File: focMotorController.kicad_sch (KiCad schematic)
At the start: 0 parts

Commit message: Start creating schematic
Currently includes:
- Power input circuitry and filtering
- Logic: microcontroller and encoder connection
- Level shifters for encoder
- Status LEDs
- Output MOSFETs
- MOSFET gate drivers with appropriate filtering (I think...)

A few other things are a work-in-porogress, like current sensing.
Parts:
- added A1: Arduino Nano RP2040 Connect, Module:Arduino_Nano, symbol MCU_Module:Arduino_Nano_RP2040_Connect
- added C1: 470uF electrolytic, symbol Device:C
- added C2: 0.1uF ceramic, symbol Device:C
- added C3: Bootstrap A 0.1uF/25v, symbol Device:C
- added C4: Bootstrap B 0.1uF/25v, symbol Device:C
- added C5: Bootstrap C 0.1uF/25v, symbol Device:C
- added C6: Deboupling B 1uF/25V, symbol Device:C
- added C7: Deboupling A 1uF/25V, symbol Device:C
- added C8: Deboupling C 1uF/25V, symbol Device:C
- added D1: SMAJ15A - TVS diode for voltage spike protection, Diode_SMD:D_SMA, symbol Diode:SMAJ15A
- added D2, D7, D8, D9: STPS20L15D, Footprints:STPS20L15D, symbol Device:D
- added D3: Power LED (red), symbol Device:LED
- added D4: Status LED 1 (green), symbol Device:LED
- added D5: Status LED 2 (green), symbol Device:LED
- added D6: Status LED 3 (green), symbol Device:LED
- added F1: Resettable polyfuse for overcurrent protection, symbol Device:Polyfuse
- added J2: JST-PH encoder connection, symbol Connector:Conn_01x06_Pin
- added P1: WJ128V-5.0-3P, Footprints:WJ128V-5.0-3P, symbol WJ128V-5.0-3P:WJ128V-5.0-3P
- added P2: Power input, Footprints:WJ128V-5.0-2P, symbol WJ128V-5.0-2P:WJ128V-5.0-2P
- added R1: 3.3k, symbol Device:R_Small
- added R10: Gate BL 20ohm, symbol Device:R
- added R11, R13, R7, R8: Pulldown 47k, symbol Device:R_Small
- added R12: Gate CH 20ohm, symbol Device:R
- added R19: Gate AL 20ohm, symbol Device:R
- added R2: 2k, symbol Device:R_Small
- added R20: Gate CL 20ohm, symbol Device:R
- added R22: Gate AH 20ohm, symbol Device:R
- added R3: 620ohm, symbol Device:R_Small
- added R4, R5, R6: 100ohm, symbol Device:R_Small
- added R9: Gate BH 20ohm, symbol Device:R
- added U1, U2: 74LVC2T45DC, Package_SO:VSSOP-8_2.3x2mm_P0.5mm, symbol Logic_LevelTranslator:74LVC2T45DC
- added U10: IR2104 Gate Driver B, symbol Driver_FET:IR2104
- added U11: IR2104 Gate Driver C, symbol Driver_FET:IR2104
- added U3: MOSFET A low, Footprints:STP55NF06L, symbol STP55NF06L:STP55NF06L
- added U4: MOSFET B low, Footprints:STP55NF06L, symbol STP55NF06L:STP55NF06L
- added U5: MOSFET C low, Footprints:STP55NF06L, symbol STP55NF06L:STP55NF06L
- added U6: MOSFET A high, Footprints:STP55NF06L, symbol STP55NF06L:STP55NF06L
- added U7: MOSFET B high, Footprints:STP55NF06L, symbol STP55NF06L:STP55NF06L
- added U8: MOSFET C high, Footprints:STP55NF06L, symbol STP55NF06L:STP55NF06L
- added U9: IR2104 Gate Driver A, symbol Driver_FET:IR2104
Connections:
- new net: D2.2 (A), F1.2
- new net: R20.1, U11.5 (LO)
- new net: D3.2 (A), R3.2
- new net: R19.1, U9.5 (LO)
- new net: D6.2 (A), R6.2
- new net: J2.5 (Motor_Temperature), R1.1
- new net: A1.19 (A0), R1.2, R2.2
- new net: D4.2 (A), R4.2
- new net: C1.1, C2.2
- new net: D5.2 (A), R5.2
- new net: R10.1, U10.5 (LO)
- new net: R12.1, U11.7 (HO)
- new net: C5.1, D9.1 (K), U11.8 (VB)
- new net: R9.1, U10.7 (HO)
- new net: C4.1, D8.1 (K), U10.8 (VB)
- new net: C3.1, D7.1 (K), U9.8 (VB)
- new net: R22.1, U9.7 (HO)
- new net +12V: F1.1, P2.1
- new net 3.3VDD: A1.17 (3V3), U1.1 (VCCA), U2.1 (VCCA)
- new net 5VDD: A1.27 (VUSB/5V), J2.6 (+5V), R3.1, U1.8 (VCCB), U2.8 (VCCB)
- new net AHighGate: R22.2, U6.1
- new net ALowGate: R19.2, U3.1
- new net BHighGate: R9.2, U7.1
- new net BLowGate: R10.2, U4.1
- new net CHighGate: R12.2, U8.1
- new net CLowGate: R20.2, U5.1
- new net Enable: A1.14 (D11/COPI), C6.1, C8.1, R13.2, U10.3 (~{SD}), U11.3 (~{SD}), U9.3 (~{SD})
- new net EncLogicA: A1.5 (D2), U1.3 (2A)
- new net EncLogicB: A1.6 (D3), U2.2 (1A)
- new net EncLogicC: A1.7 (D4), U2.3 (2A)
- new net EncoderA: J2.4 (Encoder_A), U1.6 (2B)
- new net EncoderB: J2.3 (Encoder_B), U2.7 (1B)
- new net EncoderC: J2.2 (Encoder_C_/_Index), U2.6 (2B)
- new net GND: A1.29 (GND), A1.4 (GND), C2.1, C6.2, C7.2, C8.2, D1.1 (A1), D3.1 (K), D4.1 (K), D5.1 (K), D6.1 (K), J2.1 (Ground), P2.2, R11.1, R13.1, R2.1, R7.1, R8.1, U1.4 (GND), U1.5 (DIR), U10.4 (COM), U11.4 (COM), U2.4 (GND), U2.5 (DIR), U3.3, U4.3, U5.3, U9.4 (COM)
- new net PVIN: A1.30 (VIN), C1.2, C7.1, D1.2 (A2), D2.1 (K), D7.2 (A), D8.2 (A), D9.2 (A), U10.1 (VCC), U11.1 (VCC), U6.2, U7.2, U8.2, U9.1 (VCC)
- new net PhaseA: A1.11 (D8), R7.2, U9.2 (IN)
- new net PhaseAOut: C3.2, P1.1, U3.2, U6.3, U9.6 (VS)
- new net PhaseB: A1.12 (D9), R8.2, U10.2 (IN)
- new net PhaseBOut: C4.2, P1.2, U10.6 (VS), U4.2, U7.3
- new net PhaseC: A1.13 (D10/CS), R11.2, U11.2 (IN)
- new net PhaseCOut: C5.2, P1.3, U11.6 (VS), U5.2, U8.3
- new net Status1: A1.8 (D5), R4.1
- new net Status2: A1.9 (D6), R5.1
- new net Status3: A1.10 (D7), R6.1
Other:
- note added: "Can handle 5-18V input"
- note added: "DIR = LOW passes data B -> A"
- note added: "For my own reference lol V_out = V_in * R_2 / (R_1 + R_2) For 5V to 3.3V level shifting, R_2 / (R_1 + R_2) = 3.3 / 5, so e.g R_1 = 3.3k / R_2 = 2k"
- note added: "Level shifters (forced 5V to 3.3V)"
- note added: "Logic"
- note added: "MOSFET Gate Drivers"
- note added: "Note: Gate resistors should be placed directly before the MOSFET gate pin to reduce PCB loop inductance"
- note added: "Output MOSFETs"
- note added: "Power input"
- note added: "Regulated outputs"
- note added: "Should handle ~10A hold current"
- note added: "Status LEDs"
- note added: "VCC deboupling and bootstrap capacitors should also be directly next to the gate driver ICs"

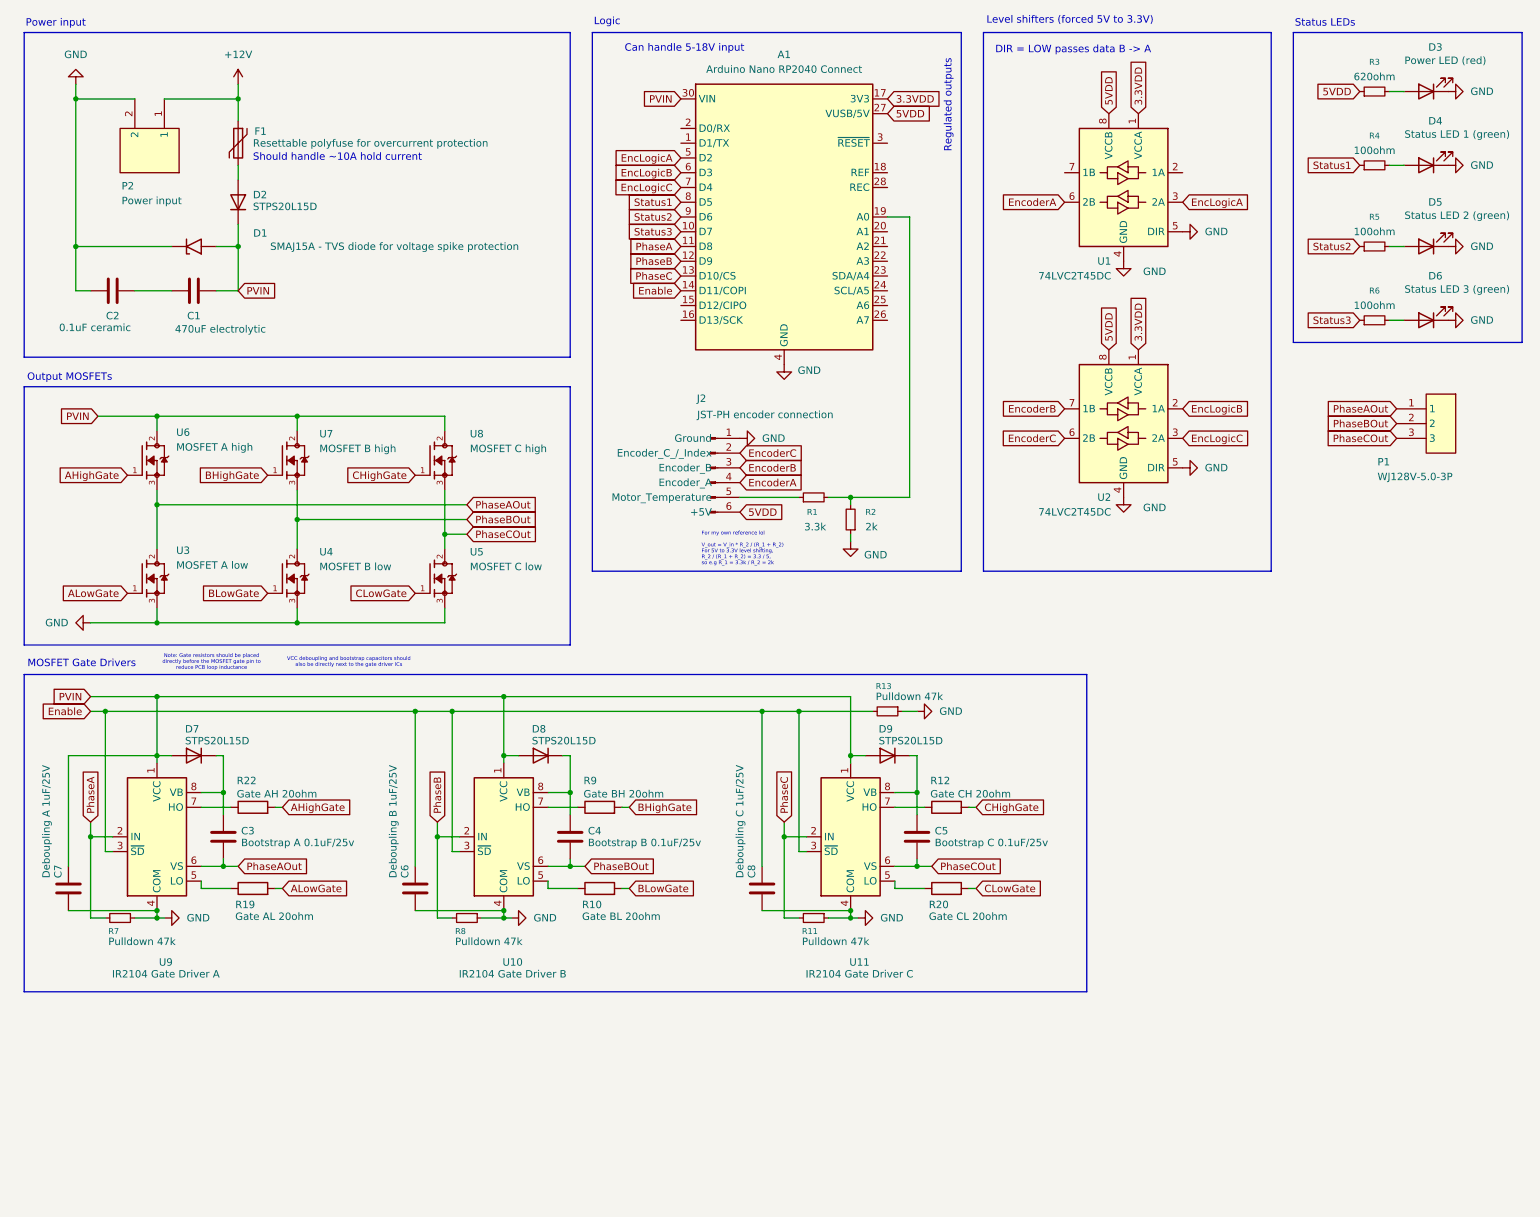
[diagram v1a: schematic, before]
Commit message: Add current sensing circuitry
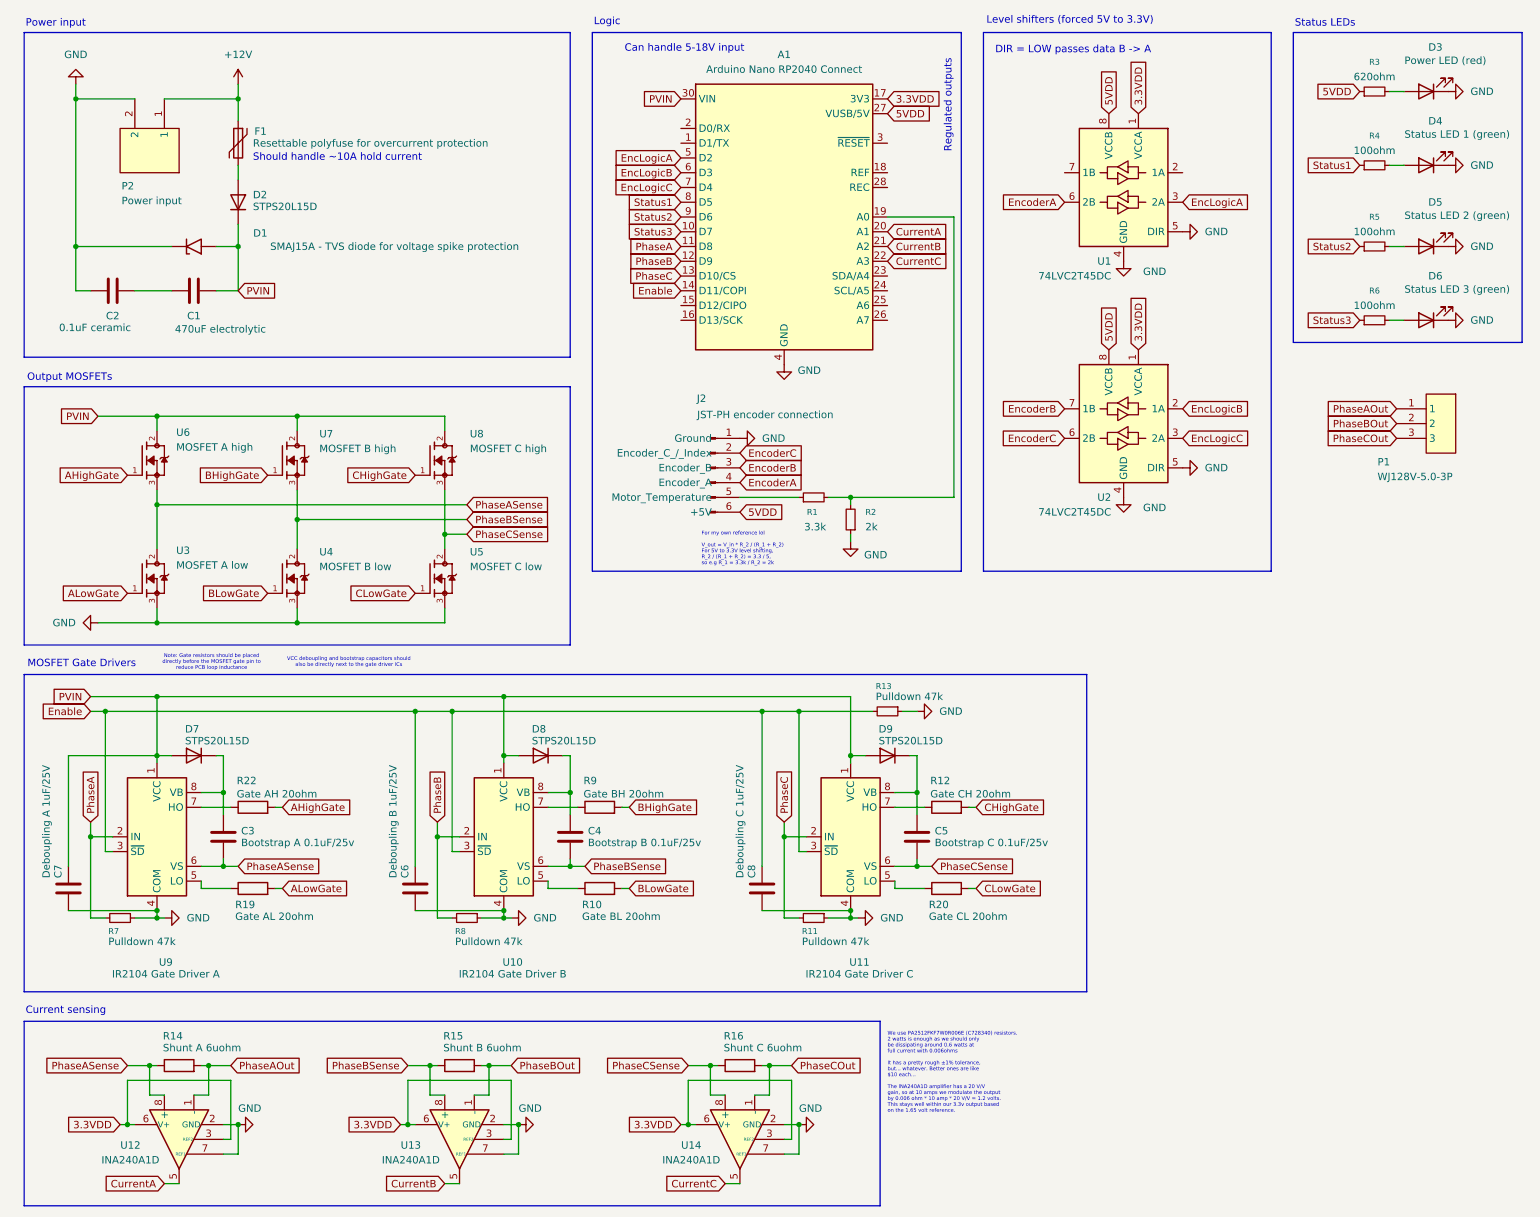
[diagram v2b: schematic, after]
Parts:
- added R14: Shunt A 6uohm, Resistor_SMD:R_2512_6332Metric, symbol Device:R
- added R15: Shunt B 6uohm, Resistor_SMD:R_2512_6332Metric, symbol Device:R
- added R16: Shunt C 6uohm, Resistor_SMD:R_2512_6332Metric, symbol Device:R
- added U12, U13, U14: INA240A1D, Package_SO:SOIC-8_3.9x4.9mm_P1.27mm, symbol Amplifier_Current:INA240A1D
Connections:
- net 3.3VDD: now also U12.3 (REF2), U12.6 (V+), U13.3 (REF2), U13.6 (V+), U14.3 (REF2), U14.6 (V+)
- net GND: now also U12.2 (GND), U12.4 (GND), U12.7 (REF1), U13.2 (GND), U13.4 (GND), U13.7 (REF1), U14.2 (GND), U14.4 (GND), U14.7 (REF1)
- net PhaseAOut: now also R14.2, U12.1 (-); no longer C3.2, U3.2, U6.3, U9.6 (VS)
- net PhaseBOut: now also R15.2, U13.1 (-); no longer C4.2, U10.6 (VS), U4.2, U7.3
- net PhaseCOut: now also R16.2, U14.1 (-); no longer C5.2, U11.6 (VS), U5.2, U8.3
- net CurrentA: now reaches A1.20 (A1)
- net CurrentA: now also U12.5
- net CurrentB: now reaches A1.21 (A2)
- net CurrentB: now also U13.5
- net CurrentC: now reaches A1.22 (A3)
- net CurrentC: now also U14.5
- new net PhaseASense: C3.2, R14.1, U12.8 (+), U3.2, U6.3, U9.6 (VS)
- new net PhaseBSense: C4.2, R15.1, U10.6 (VS), U13.8 (+), U4.2, U7.3
- new net PhaseCSense: C5.2, R16.1, U11.6 (VS), U14.8 (+), U5.2, U8.3
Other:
- note added: "Current sensing"
- note added: "We use PA2512FKF7W0R006E (C728340) resistors. 2 watts is enough as we should only be dissipating around 0.6 watts at full current with 0.006ohms It has a pretty rough ±1% tolerance, but... whatever. Better ones are like $10 each... The INA240A1D amplifier has a 20 V/V gain, so at 10 amps we modulate the output by 0.006 ohm * 10 amp * 20 V/V = 1.2 volts. This stays well within our 3.3v output base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"

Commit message: Finish initial routing
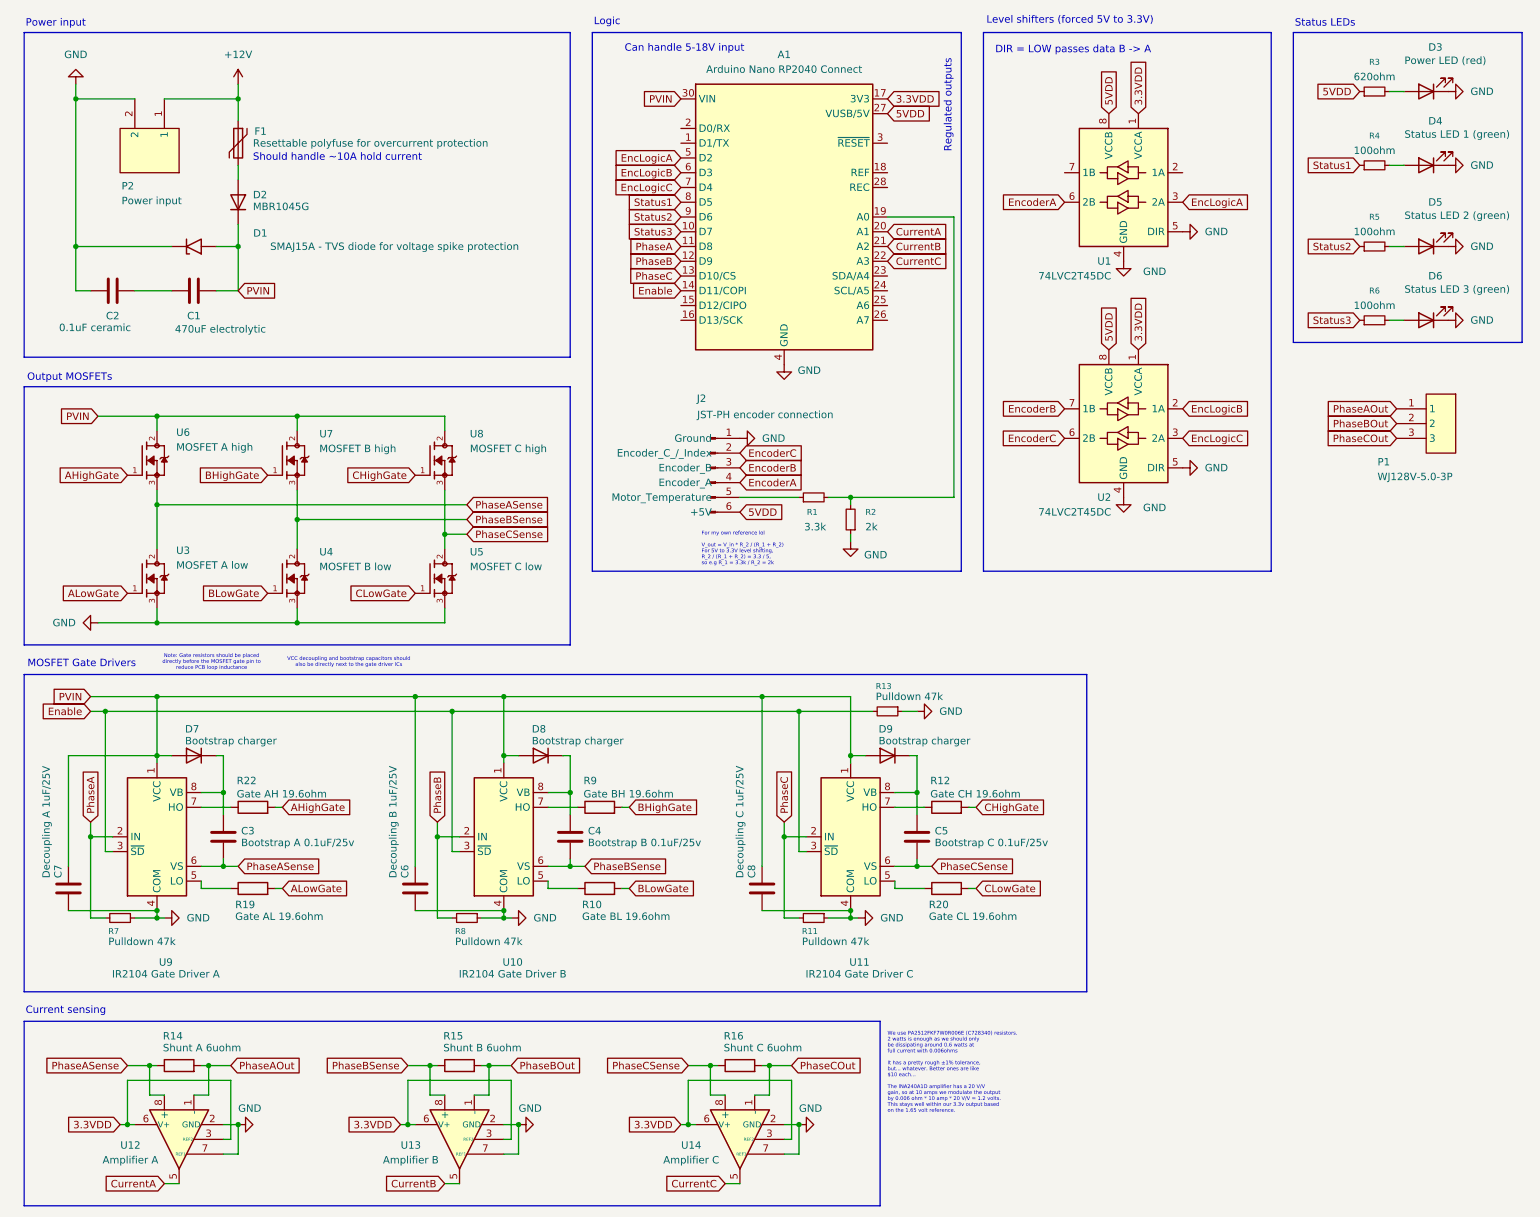
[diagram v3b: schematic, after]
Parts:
- C1: footprint (none) -> Capacitor_THT:CP_Radial_D8.0mm_P3.50mm
- C2, C3, C4, C5: footprint (none) -> Capacitor_THT:C_Disc_D5.0mm_W2.5mm_P5.00mm
- C6: value Deboupling B 1uF/25V -> Decoupling B 1uF/25V; footprint (none) -> Capacitor_THT:CP_Radial_D5.0mm_P2.00mm
- C7: value Deboupling A 1uF/25V -> Decoupling A 1uF/25V; footprint (none) -> Capacitor_THT:CP_Radial_D5.0mm_P2.00mm
- C8: value Deboupling C 1uF/25V -> Decoupling C 1uF/25V; footprint (none) -> Capacitor_THT:CP_Radial_D5.0mm_P2.00mm
- D2: value STPS20L15D -> MBR1045G; footprint Footprints:STPS20L15D -> Package_TO_SOT_THT:TO-220-2_Vertical
- D3, D4, D5, D6, R1, R11, R13, R2, R3, R4, R5, R6, R7, R8: footprint (none) -> LED_SMD:LED_1206_3216Metric
- D7, D8, D9: value STPS20L15D -> Bootstrap charger; footprint Footprints:STPS20L15D -> Diode_SMD:D_SOD-123
- F1: footprint (none) -> Footprints:A16-1000
- J2: footprint (none) -> Connector_JST:JST_PH_S6B-PH-K_1x06_P2.00mm_Horizontal
- R10: value Gate BL 20ohm -> Gate BL 19.6ohm; footprint (none) -> Resistor_SMD:R_1206_3216Metric
- R12: value Gate CH 20ohm -> Gate CH 19.6ohm; footprint (none) -> Resistor_SMD:R_1206_3216Metric
- R19: value Gate AL 20ohm -> Gate AL 19.6ohm; footprint (none) -> Resistor_SMD:R_1206_3216Metric
- R20: value Gate CL 20ohm -> Gate CL 19.6ohm; footprint (none) -> Resistor_SMD:R_1206_3216Metric
- R22: value Gate AH 20ohm -> Gate AH 19.6ohm; footprint (none) -> Resistor_SMD:R_1206_3216Metric
- R9: value Gate BH 20ohm -> Gate BH 19.6ohm; footprint (none) -> Resistor_SMD:R_1206_3216Metric
- U10, U11, U9: footprint (none) -> Footprints:IR2104SPBF
- U12: value INA240A1D -> Amplifier A
- U13: value INA240A1D -> Amplifier B
- U14: value INA240A1D -> Amplifier C
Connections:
- net Enable: no longer C6.1, C8.1
- net PVIN: now also C6.1, C8.1
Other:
- note added: "VCC decoupling and bootstrap capacitors should also be directly next to the gate driver ICs"
- note removed: "VCC deboupling and bootstrap capacitors should also be directly next to the gate driver ICs"

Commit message: Update schematics with remaining JLCPCB parts, finish BOM, and export manufacturing files
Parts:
- R1, R11, R13, R2, R3, R4, R5, R6, R7, R8: footprint LED_SMD:LED_1206_3216Metric -> Resistor_SMD:R_1206_3216Metric
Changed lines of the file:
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@@
 			)
 		)
-		(property "Footprint" "LED_SMD:LED_1206_3216Metric"
+		(property "Footprint" "Resistor_SMD:R_1206_3216Metric"
 			(at 151.13 97.79 0)
 			(effects
@@
 			)
 		)
-		(property "Footprint" "LED_SMD:LED_1206_3216Metric"
+		(property "Footprint" "Resistor_SMD:R_1206_3216Metric"
 			(at 247.65 40.64 0)
 			(effects
@@
 			)
 		)
-		(property "Footprint" "LED_SMD:LED_1206_3216Metric"
+		(property "Footprint" "Resistor_SMD:R_1206_3216Metric"
 			(at 157.48 101.6 0)
 			(effects
@@
 			)
 		)
-		(property "Footprint" "LED_SMD:LED_1206_3216Metric"
+		(property "Footprint" "Resistor_SMD:R_1206_3216Metric"
 			(at 31.75 170.18 0)
 			(effects
@@
 			)
 		)
-		(property "Footprint" "LED_SMD:LED_1206_3216Metric"
+		(property "Footprint" "Resistor_SMD:R_1206_3216Metric"
 			(at 247.65 54.61 0)
 			(effects
@@
 			)
 		)
-		(property "Footprint" "LED_SMD:LED_1206_3216Metric"
+		(property "Footprint" "Resistor_SMD:R_1206_3216Metric"
 			(at 151.13 170.18 0)
 			(effects
@@
 			)
 		)
-		(property "Footprint" "LED_SMD:LED_1206_3216Metric"
+		(property "Footprint" "Resistor_SMD:R_1206_3216Metric"
 			(at 247.65 27.94 0)
 			(effects
@@
 			)
 		)
-		(property "Footprint" "LED_SMD:LED_1206_3216Metric"
+		(property "Footprint" "Resistor_SMD:R_1206_3216Metric"
 			(at 163.83 134.62 0)
 			(effects
@@
 			)
 		)
-		(property "Footprint" "LED_SMD:LED_1206_3216Metric"
+		(property "Footprint" "Resistor_SMD:R_1206_3216Metric"
 			(at 247.65 67.31 0)
 			(effects
@@
 			)
 		)
-		(property "Footprint" "LED_SMD:LED_1206_3216Metric"
+		(property "Footprint" "Resistor_SMD:R_1206_3216Metric"
 			(at 91.44 170.18 0)
 			(effects
